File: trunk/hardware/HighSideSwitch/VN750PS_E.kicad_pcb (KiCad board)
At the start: 2 copper layers, 17 x 22 mm, 8 parts, among them P1 CONN_01X08, P2 CONN_01X02, Q1 VN750PS_E

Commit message: 
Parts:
- D1: value D -> (none)
- P1: value CONN_01X08 -> (none)
- P2: value CONN_01X02 -> (none)
- Q1: value VN750PS_E -> (none)
- R1: value 130 -> (none)
- R2, R3, R4: value 10k -> (none)
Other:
- copper layers 2 -> 4
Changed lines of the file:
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@@
   (page A4)
   (layers
-    (0 F.Cu signal)
-    (31 B.Cu signal)
-    (32 B.Adhes user)
-    (33 F.Adhes user)
-    (34 B.Paste user)
-    (35 F.Paste user)
-    (36 B.SilkS user)
-    (37 F.SilkS user)
-    (38 B.Mask user)
-    (39 F.Mask user)
-    (40 Dwgs.User user)
-    (41 Cmts.User user)
-    (42 Eco1.User user)
-    (43 Eco2.User user)
-    (44 Edge.Cuts user)
-    (45 Margin user)
-    (46 B.CrtYd user)
-    (47 F.CrtYd user)
-    (48 B.Fab user)
-    (49 F.Fab user)
+    (15 F.Cu signal)
+	(0 B.Cu signal)
+	(1 In1.Cu signal)
+	(2 In2.Cu signal)
+	(16 B.Adhes user)
+	(17 F.Adhes user)
+	(18 B.Paste user)
+	(19 F.Paste user)
+	(20 B.SilkS user)
+	(21 F.SilkS user)
+	(22 B.Mask user)
+	(23 F.Mask user)
+	(24 Dwgs.User user)
+	(25 Cmts.User user)
+	(26 Eco1.User user)
+	(27 Eco2.User user)
+	(28 Edge.Cuts user)
   )
   (setup
@@
     (visible_elements 7FFFFFFF)
     (pcbplotparams
-      (layerselection 0x010f0_80000001)
+      (layerselection 3178497)
       (usegerberextensions true)
       (excludeedgelayer true)
@@
       (effects (font (size 1 1) (thickness 0.15)))
     )
-    (fp_text value VN750PS_E (at -1.778 -3.683 270) (layer F.Fab)
-      (effects (font (size 1 1) (thickness 0.15)))
-    )
     (fp_text user 1 (at -1.45542 -2.0066 270) (layer F.SilkS)
       (effects (font (size 0.5 0.5) (thickness 0.0625)))
@@
       (effects (font (size 1 1) (thickness 0.15)) (justify mirror))
     )
-    (fp_text value D (at 0.1524 2.37744) (layer B.Fab) hide
-      (effects (font (size 1 1) (thickness 0.15)) (justify mirror))
-    )
     (fp_line (start -3.03276 0.87376) (end -3.03276 -0.87376) (layer B.SilkS) (width 0.15))
     (pad 2 smd rect (at 1.778 -0.01868) (size 1.6 1.7) (layers B.Cu B.Paste B.Mask)
@@
       (effects (font (size 1 1) (thickness 0.15)))
     )
-    (fp_text value 130 (at -4.953 -0.0635 270) (layer F.Fab) hide
-      (effects (font (size 1 1) (thickness 0.15)))
-    )
-    (fp_line (start -2 -0.8) (end 2 -0.8) (layer F.CrtYd) (width 0.05))
-    (fp_line (start -2 0.8) (end 2 0.8) (layer F.CrtYd) (width 0.05))
-    (fp_line (start -2 -0.8) (end -2 0.8) (layer F.CrtYd) (width 0.05))
-    (fp_line (start 2 -0.8) (end 2 0.8) (layer F.CrtYd) (width 0.05))
     (fp_line (start 0.5 0.675) (end -0.5 0.675) (layer F.SilkS) (width 0.15))
     (fp_line (start -0.5 -0.675) (end 0.5 -0.675) (layer F.SilkS) (width 0.15))
@@
       (effects (font (size 1 1) (thickness 0.15)))
     )
-    (fp_text value 10k (at -4.8895 0.0635 270) (layer F.Fab) hide
-      (effects (font (size 1 1) (thickness 0.15)))
-    )
-    (fp_line (start -2 -0.8) (end 2 -0.8) (layer F.CrtYd) (width 0.05))
-    (fp_line (start -2 0.8) (end 2 0.8) (layer F.CrtYd) (width 0.05))
-    (fp_line (start -2 -0.8) (end -2 0.8) (layer F.CrtYd) (width 0.05))
-    (fp_line (start 2 -0.8) (end 2 0.8) (layer F.CrtYd) (width 0.05))
     (fp_line (start 0.5 0.675) (end -0.5 0.675) (layer F.SilkS) (width 0.15))
     (fp_line (start -0.5 -0.675) (end 0.5 -0.675) (layer F.SilkS) (width 0.15))
@@
       (effects (font (size 1 1) (thickness 0.15)))
     )
-    (fp_text value CONN_01X08 (at 0.254 -3.683 180) (layer F.Fab) hide
-      (effects (font (size 1 1) (thickness 0.15)))
-    )
-    (fp_line (start -1.5 -1.75) (end -1.5 19.55) (layer F.CrtYd) (width 0.05))
-    (fp_line (start 10.65 -1.75) (end 10.65 19.55) (layer F.CrtYd) (width 0.05))
-    (fp_line (start -1.5 -1.75) (end 10.65 -1.75) (layer F.CrtYd) (width 0.05))
-    (fp_line (start -1.5 19.55) (end 10.65 19.55) (layer F.CrtYd) (width 0.05))
     (fp_line (start -1.3 -1.55) (end -1.3 0) (layer F.SilkS) (width 0.15))
     (fp_line (start 0 -1.55) (end -1.3 -1.55) (layer F.SilkS) (width 0.15))
@@
       (effects (font (size 1 1) (thickness 0.15)))
     )
-    (fp_text value 10k (at 5.0165 -0.1905 90) (layer F.Fab) hide
-      (effects (font (size 1 1) (thickness 0.15)))
-    )
-    (fp_line (start -2 -0.8) (end 2 -0.8) (layer F.CrtYd) (width 0.05))
-    (fp_line (start -2 0.8) (end 2 0.8) (layer F.CrtYd) (width 0.05))
-    (fp_line (start -2 -0.8) (end -2 0.8) (layer F.CrtYd) (width 0.05))
-    (fp_line (start 2 -0.8) (end 2 0.8) (layer F.CrtYd) (width 0.05))
     (fp_line (start 0.5 0.675) (end -0.5 0.675) (layer F.SilkS) (width 0.15))
     (fp_line (start -0.5 -0.675) (end 0.5 -0.675) (layer F.SilkS) (width 0.15))
@@
       (effects (font (size 1 1) (thickness 0.15)))
     )
-    (fp_text value 10k (at 5.0165 0.254 90) (layer F.Fab) hide
-      (effects (font (size 1 1) (thickness 0.15)))
-    )
-    (fp_line (start -2 -0.8) (end 2 -0.8) (layer F.CrtYd) (width 0.05))
-    (fp_line (start -2 0.8) (end 2 0.8) (layer F.CrtYd) (width 0.05))
-    (fp_line (start -2 -0.8) (end -2 0.8) (layer F.CrtYd) (width 0.05))
-    (fp_line (start 2 -0.8) (end 2 0.8) (layer F.CrtYd) (width 0.05))
     (fp_line (start 0.5 0.675) (end -0.5 0.675) (layer F.SilkS) (width 0.15))
     (fp_line (start -0.5 -0.675) (end 0.5 -0.675) (layer F.SilkS) (width 0.15))
@@
       (effects (font (size 1 1) (thickness 0.15)))
     )
-    (fp_text value CONN_01X02 (at -8.382 7.6835 90) (layer F.Fab) hide
-      (effects (font (size 1 1) (thickness 0.15)))
-    )

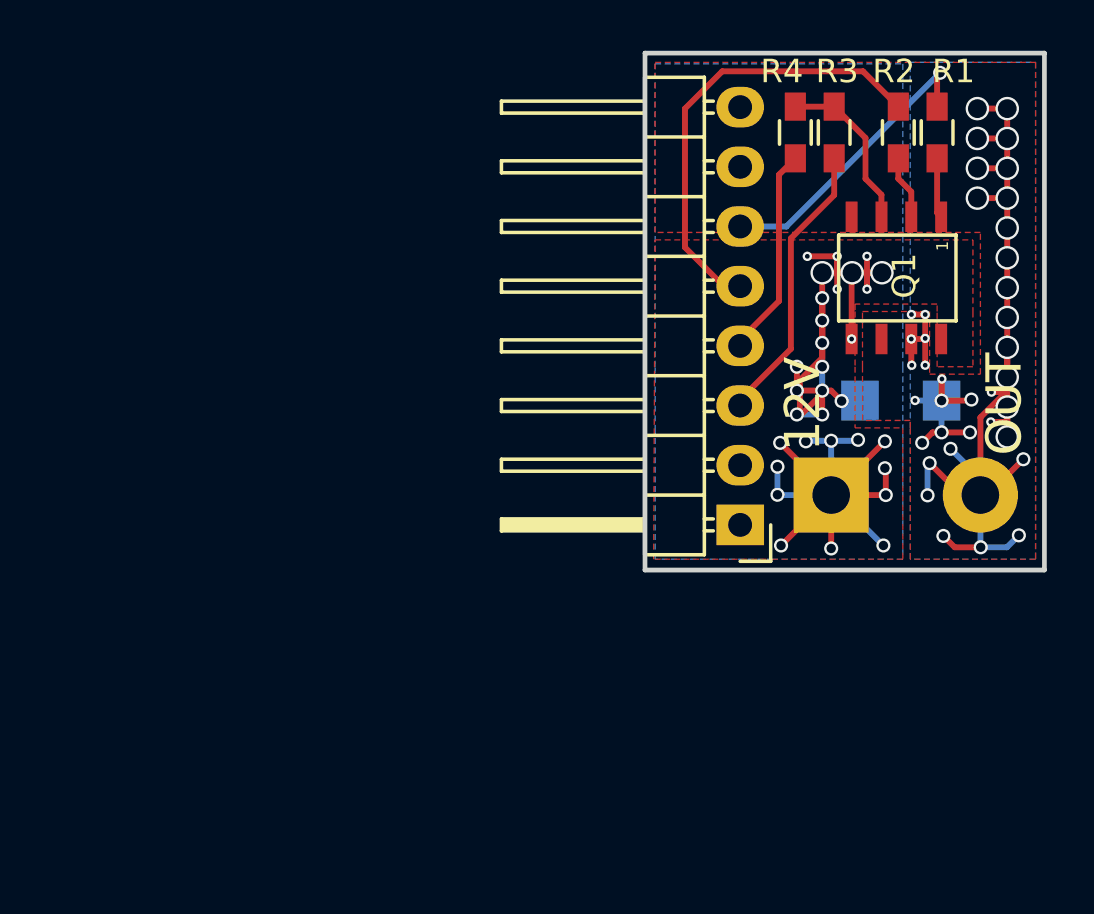
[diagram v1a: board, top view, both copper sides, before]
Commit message: 
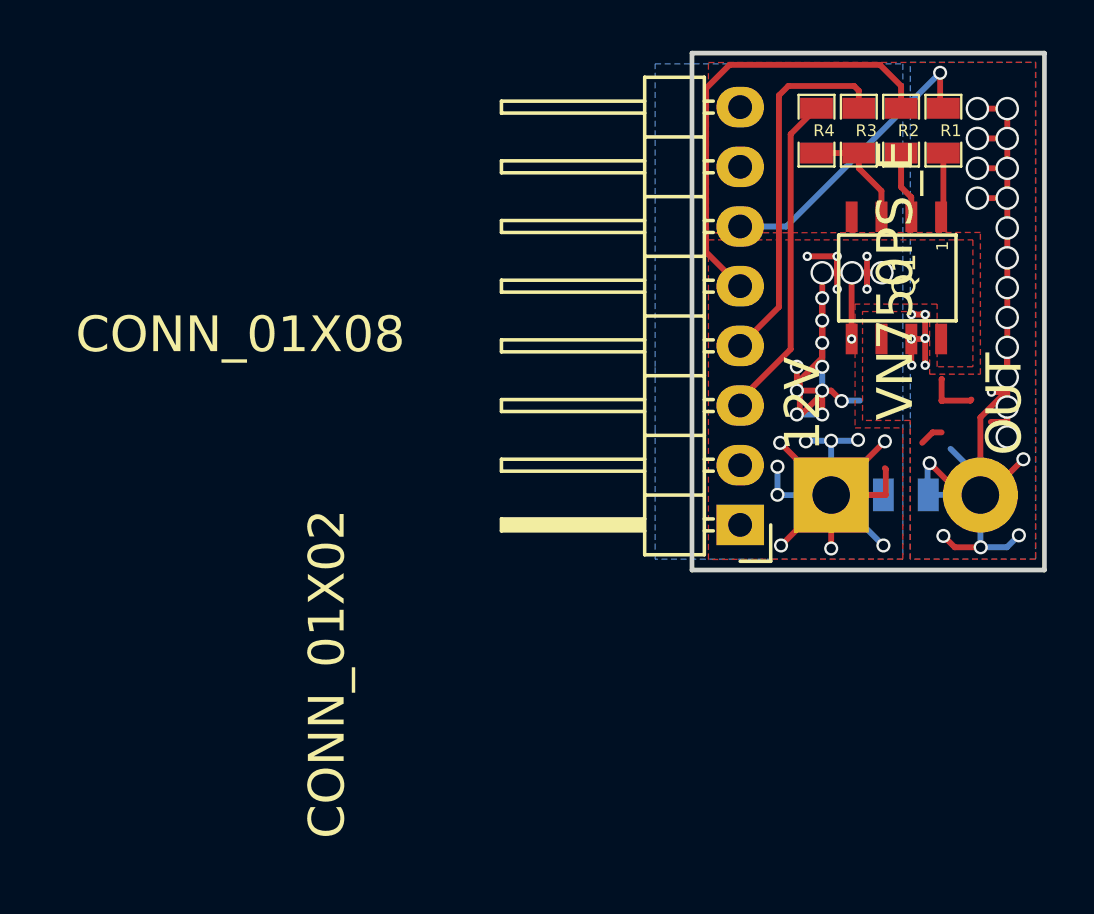
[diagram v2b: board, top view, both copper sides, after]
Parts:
- D1: value (none) -> D; footprint VN750PS_E_Vertical:US1GHE3 -> SM0805-diode
- P1: value (none) -> CONN_01X08
- P2: value (none) -> CONN_01X02
- Q1: value (none) -> VN750PS_E
- R1: value (none) -> 130; footprint Resistors_SMD:R_0603_HandSoldering -> RES_0805
- R2, R3, R4: value (none) -> 10k; footprint Resistors_SMD:R_0603_HandSoldering -> RES_0805
- moved D1 4.00 mm to (161.1, 118.8)
- moved R3 2.70 mm to (159.1, 103.3), turned to 270 degrees
- moved R4 0.76 mm to (157.3, 103.3), turned to 270 degrees
- moved R1 0.28 mm to (162.7, 103.3)
- moved R2 0.14 mm to (160.9, 103.3)
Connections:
- P1 pad 1: Net-(P1-Pad1) -> (no net)
- P1 pad 2: Net-(P1-Pad2) -> (no net)
- P1 pad 7: Net-(P1-Pad7) -> (no net)
- P1 pad 8: Net-(P1-Pad8) -> (no net)
- Q1 pad 4: Net-(Q1-Pad4) -> (no net)
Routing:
- net Net-(P1-Pad4): track 8.95 -> 15.7 mm
- net Net-(D1-Pad2): track 54.7 -> 50.0 mm, vias 38 -> 28
- net (no net): track 0.00 -> 3.26 mm
- net Net-(Q1-Pad3): track 7.17 -> 4.91 mm
- net +12V: track 59.3 -> 61.5 mm, vias 31 -> 29
- net +5V: track 12.4 -> 14.2 mm
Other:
- board size 17 x 22 mm -> 15 x 22 mm
